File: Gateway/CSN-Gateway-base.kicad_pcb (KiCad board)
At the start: 2 copper layers, 32 x 85.5 mm, 0 parts

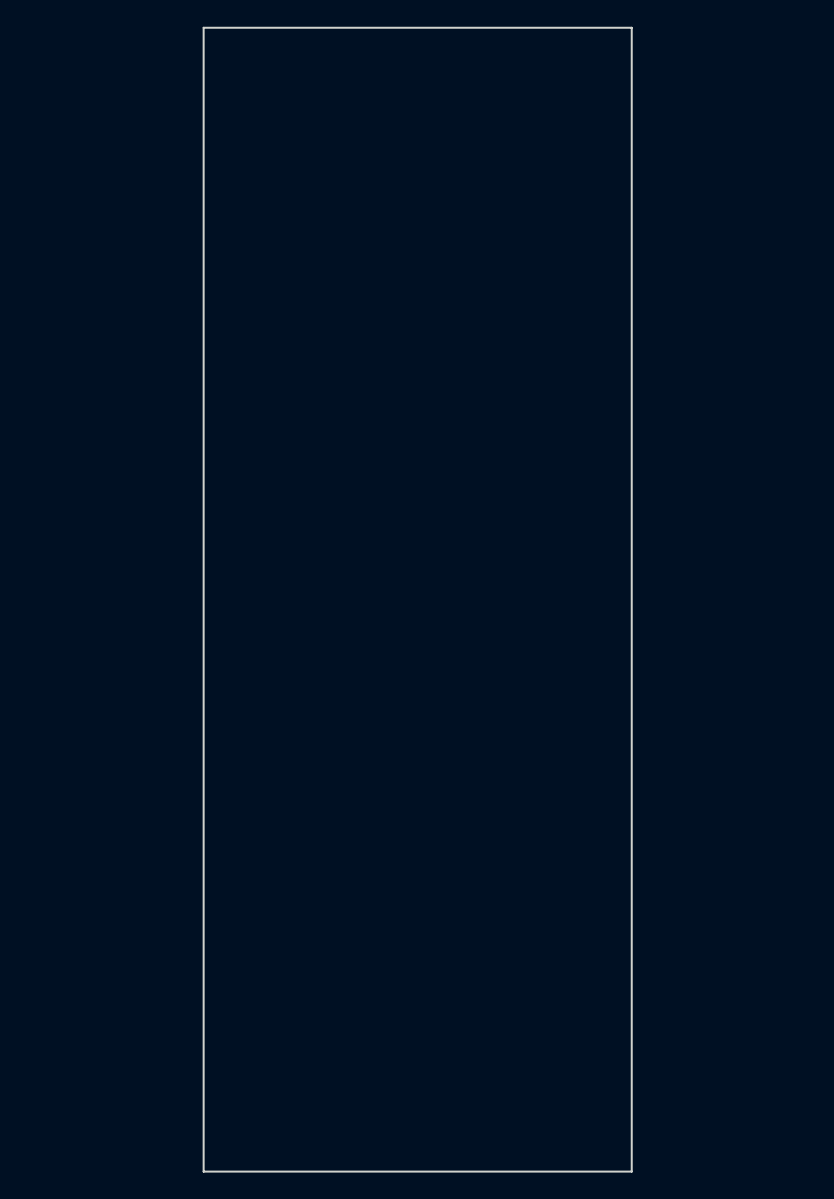
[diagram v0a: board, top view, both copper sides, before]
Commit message: add some pcb footprint
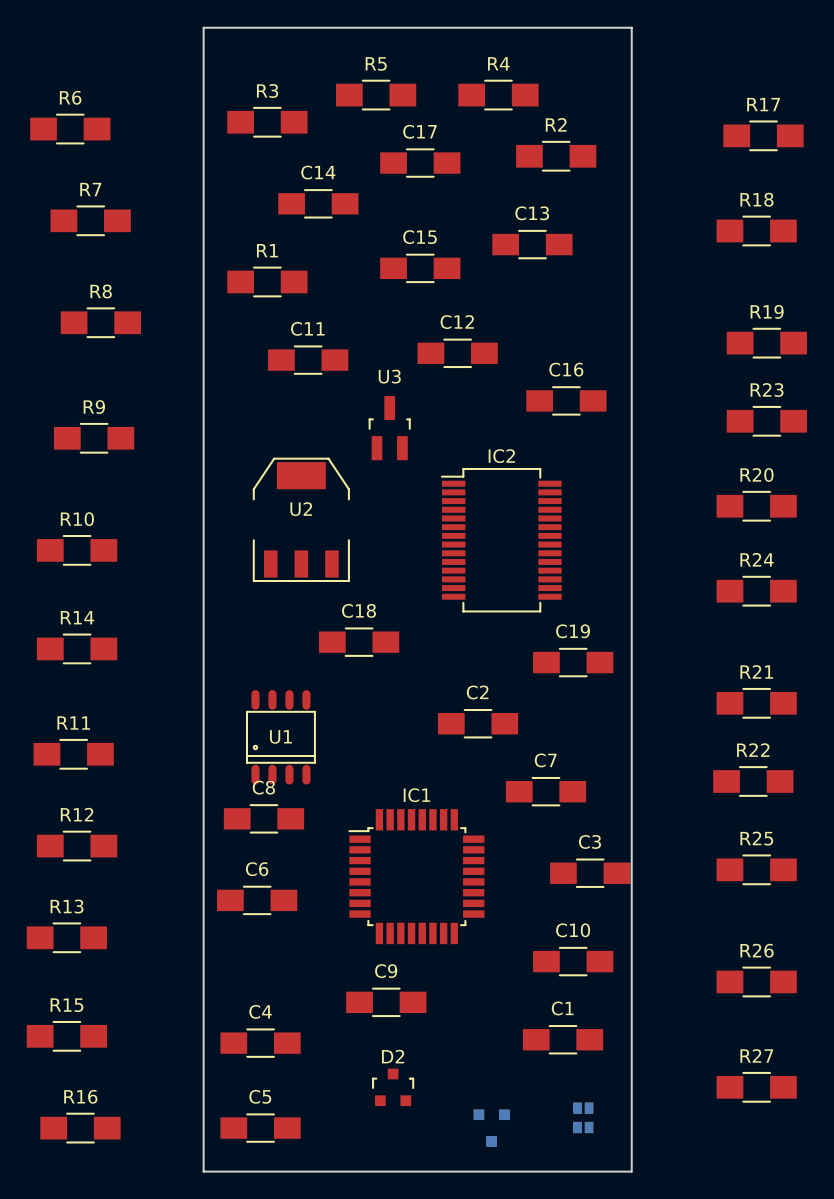
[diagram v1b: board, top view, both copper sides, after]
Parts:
- added C1: 0.1uF, Capacitors_SMD:C_1206_HandSoldering, F.Cu at (165.9, 136.1)
- added C10: 10uF, Capacitors_SMD:C_1206_HandSoldering, F.Cu at (166.6, 130.3)
- added C11: 0.1uF, Capacitors_SMD:C_1206_HandSoldering, F.Cu at (146.8, 85.3)
- added C12: 0.1uF, Capacitors_SMD:C_1206_HandSoldering, F.Cu at (158.0, 84.8)
- added C13: 10uF, Capacitors_SMD:C_1206_HandSoldering, F.Cu at (163.6, 76.7)
- added C14: 100nF, Capacitors_SMD:C_1206_HandSoldering, F.Cu at (147.6, 73.7)
- added C15: 100nF, Capacitors_SMD:C_1206_HandSoldering, F.Cu at (155.2, 78.5)
- added C16: 100nF, Capacitors_SMD:C_1206_HandSoldering, F.Cu at (166.1, 88.4)
- added C17: 10uF, Capacitors_SMD:C_1206_HandSoldering, F.Cu at (155.2, 70.6)
- added C18: 100nF, Capacitors_SMD:C_1206_HandSoldering, F.Cu at (150.6, 106.4)
- added C19: 100nF, Capacitors_SMD:C_1206_HandSoldering, F.Cu at (166.6, 108.0)
- added C2: 0.1uF, Capacitors_SMD:C_1206_HandSoldering, F.Cu at (159.5, 112.5)
- added C3: 22pF, Capacitors_SMD:C_1206_HandSoldering, F.Cu at (167.9, 123.7)
- added C4: 22pF, Capacitors_SMD:C_1206_HandSoldering, F.Cu at (143.3, 136.4)
- added C5: 10uF, Capacitors_SMD:C_1206_HandSoldering, F.Cu at (143.3, 142.7)
- added C6: 10uF, Capacitors_SMD:C_1206_HandSoldering, F.Cu at (143.0, 125.7)
- added C7: 10uF, Capacitors_SMD:C_1206_HandSoldering, F.Cu at (164.6, 117.6)
- added C8: 0.1uF, Capacitors_SMD:C_1206_HandSoldering, F.Cu at (143.5, 119.6)
- added C9: 10uF, Capacitors_SMD:C_1206_HandSoldering, F.Cu at (152.7, 133.3)
- added D1: LED_RABG, footprints:LED-0606, B.Cu at (167.4, 142.0)
- added D2: TL431, TO_SOT_Packages_SMD:SOT-23, F.Cu at (153.2, 139.7)
- added IC1: ATMEGA328-A, Housings_QFP:TQFP-32_7x7mm_Pitch0.8mm, F.Cu at (154.9, 124.0)
- added IC2: FT232RL, Housings_SSOP:SSOP-28_5.3x10.2mm_Pitch0.65mm, F.Cu at (161.3, 98.8)
- added Q1: 2N2222, TO_SOT_Packages_SMD:SOT-23, B.Cu at (160.5, 142.7)
- added R1: 10K, Resistors_SMD:R_1206_HandSoldering, F.Cu at (143.8, 79.5)
- added R10: 10K, Resistors_SMD:R_1206_HandSoldering, F.Cu at (129.5, 99.6)
- added R11: 10K, Resistors_SMD:R_1206_HandSoldering, F.Cu at (129.3, 114.8)
- added R12: 10K, Resistors_SMD:R_1206_HandSoldering, F.Cu at (129.5, 121.7)
- added R13: 10K, Resistors_SMD:R_1206_HandSoldering, F.Cu at (128.8, 128.5)
- added R14: 10KR, Resistors_SMD:R_1206_HandSoldering, F.Cu at (129.5, 106.9)
- added R15: 10K, Resistors_SMD:R_1206_HandSoldering, F.Cu at (128.8, 135.9)
- added R16: 100, Resistors_SMD:R_1206_HandSoldering, F.Cu at (129.8, 142.7)
- added R17: 20K, Resistors_SMD:R_1206_HandSoldering, F.Cu at (180.8, 68.6)
- added R18: 20K, Resistors_SMD:R_1206_HandSoldering, F.Cu at (180.3, 75.7)
- added R19: 120, Resistors_SMD:R_1206_HandSoldering, F.Cu at (181.1, 84.1)
- added R2: 33, Resistors_SMD:R_1206_HandSoldering, F.Cu at (165.4, 70.1)
- added R20: 4k7, Resistors_SMD:R_1206_HandSoldering, F.Cu at (180.3, 96.3)
- added R21: 10k, Resistors_SMD:R_1206_HandSoldering, F.Cu at (180.3, 111.0)
- added R22: 100, Resistors_SMD:R_1206_HandSoldering, F.Cu at (180.1, 116.8)
- added R23: 100, Resistors_SMD:R_1206_HandSoldering, F.Cu at (181.1, 89.9)
- added R24: 1.5K, Resistors_SMD:R_1206_HandSoldering, F.Cu at (180.3, 102.6)
- added R25: 27.4K, Resistors_SMD:R_1206_HandSoldering, F.Cu at (180.3, 123.4)
- added R26: 27.4K, Resistors_SMD:R_1206_HandSoldering, F.Cu at (180.3, 131.8)
- added R27: 10K, Resistors_SMD:R_1206_HandSoldering, F.Cu at (180.3, 139.7)
- added R3: 10K, Resistors_SMD:R_1206_HandSoldering, F.Cu at (143.8, 67.6)
- added R4: 10K, Resistors_SMD:R_1206_HandSoldering, F.Cu at (161.0, 65.5)
- added R5: 33, Resistors_SMD:R_1206_HandSoldering, F.Cu at (151.9, 65.5)
- added R6: 10K, Resistors_SMD:R_1206_HandSoldering, F.Cu at (129.0, 68.1)
- added R7: 10K, Resistors_SMD:R_1206_HandSoldering, F.Cu at (130.6, 74.9)
- added R8: 33, Resistors_SMD:R_1206_HandSoldering, F.Cu at (131.3, 82.5)
- added R9: 10K, Resistors_SMD:R_1206_HandSoldering, F.Cu at (130.8, 91.2)
- added U1: MAX485CSA, Power_Integrations:SO-8, F.Cu at (144.8, 113.5)
- added U2: AMS1117-3.3V, TO_SOT_Packages_SMD:SOT-223, F.Cu at (146.3, 97.3)
- added U3: ATSHA204A, TO_SOT_Packages_SMD:SOT-23_Handsoldering, F.Cu at (152.9, 90.4)

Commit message: change to 0806
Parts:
- C1, C10, C11, C12, C13, C14, C15, C16, C17, C18, C19, C2, C3, C4, C5, C6, C7, C8, C9: footprint Capacitors_SMD:C_1206_HandSoldering -> Capacitors_SMD:C_0805_HandSoldering
- R1, R10, R11, R12, R13, R14, R15, R16, R17, R18, R19, R2, R20, R21, R22, R23, R24, R25, R26, R27, R3, R4, R5, R6, R7, R8, R9: footprint Resistors_SMD:R_1206_HandSoldering -> Resistors_SMD:R_0805_HandSoldering
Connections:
- IC1 pad 13: CE -> (no net)
- IC1 pad 14: CSN -> (no net)
- IC1 pad 15: MOSI -> (no net)
- IC1 pad 16: MISO -> (no net)
- IC1 pad 17: SCK -> (no net)
- IC1 pad 22: Net-(IC1-Pad22) -> (no net)
- IC1 pad 28: SCL -> (no net)
- IC1 pad 32: IRQ -> (no net)
- IC2 pad 10: Net-(IC2-Pad10) -> (no net)
- IC2 pad 11: Net-(IC2-Pad11) -> (no net)
- IC2 pad 12: Net-(IC2-Pad12) -> (no net)
- IC2 pad 13: Net-(IC2-Pad13) -> (no net)
- IC2 pad 14: Net-(IC2-Pad14) -> (no net)
- IC2 pad 15: Net-(IC2-Pad15) -> (no net)
- IC2 pad 16: Net-(IC2-Pad16) -> (no net)
- IC2 pad 17: Net-(IC2-Pad17) -> (no net)
- IC2 pad 22: Net-(IC2-Pad22) -> (no net)
- IC2 pad 23: Net-(IC2-Pad23) -> (no net)
- IC2 pad 27: Net-(IC2-Pad27) -> (no net)
- IC2 pad 28: Net-(IC2-Pad28) -> (no net)
- IC2 pad 3: Net-(IC2-Pad3) -> (no net)
- IC2 pad 6: Net-(IC2-Pad6) -> (no net)
- IC2 pad 9: Net-(IC2-Pad9) -> (no net)
- R20 pad 1: Net-(P1-Pad1) -> (no net)

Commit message: Split project into 2 sch + 2 pcb (screen + base)
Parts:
- removed C15, C19: 100nF, Capacitors_SMD:C_0805_HandSoldering
- removed C2: 0.1uF, Capacitors_SMD:C_0805_HandSoldering
- removed D1: LED_RABG, footprints:LED-0606
- removed IC2: FT232RL, Housings_SSOP:SSOP-28_5.3x10.2mm_Pitch0.65mm
- removed R15, R27: 10K, Resistors_SMD:R_0805_HandSoldering
- removed R16, R22, R23: 100, Resistors_SMD:R_0805_HandSoldering
- removed R20: 4k7, Resistors_SMD:R_0805_HandSoldering
- removed R21: 10k, Resistors_SMD:R_0805_HandSoldering
- added C20: 10uF, Capacitors_SMD:C_0805_HandSoldering, F.Cu at (169.4, 150.6)
- added P3: CONN_ICSP, Pin_Headers:Pin_Header_Straight_2x03, F.Cu at (179.3, 144.3)
- added P8: CONN_NRF24L01, mysensors_radios:NRF24L01, F.Cu at (128.5, 139.4)
- added R28: 33, Resistors_SMD:R_0805_HandSoldering, F.Cu at (142.2, 151.9)
- added R29: 10K, Resistors_SMD:R_0805_HandSoldering, F.Cu at (180.6, 109.2)
- added R30: 10K, Resistors_SMD:R_0805_HandSoldering, F.Cu at (179.6, 90.4)
- added Y1: Crystal, mysensors_obscurities:XTAL_3.2x1.5mm, F.Cu at (179.8, 96.0)
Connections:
- net Net-(P9-Pad1) renamed RS485-A
- net Net-(P9-Pad2) renamed RS485-B
- IC1 pad 10: Net-(IC1-Pad10) -> (no net)
- IC1 pad 11: Net-(IC1-Pad11) -> (no net)
- IC1 pad 12: BTN1 -> (no net)
- IC1 pad 13: (no net) -> CE
- IC1 pad 14: (no net) -> CSN
- IC1 pad 15: (no net) -> MOSI
- IC1 pad 16: (no net) -> MISO
- IC1 pad 17: (no net) -> SCK
- IC1 pad 22: (no net) -> A3
- IC1 pad 25: BTN2 -> (no net)
- IC1 pad 26: Net-(IC1-Pad26) -> (no net)
- IC1 pad 30: RXI -> (no net)
- IC1 pad 31: TXO -> (no net)
- IC1 pad 32: (no net) -> IRQ

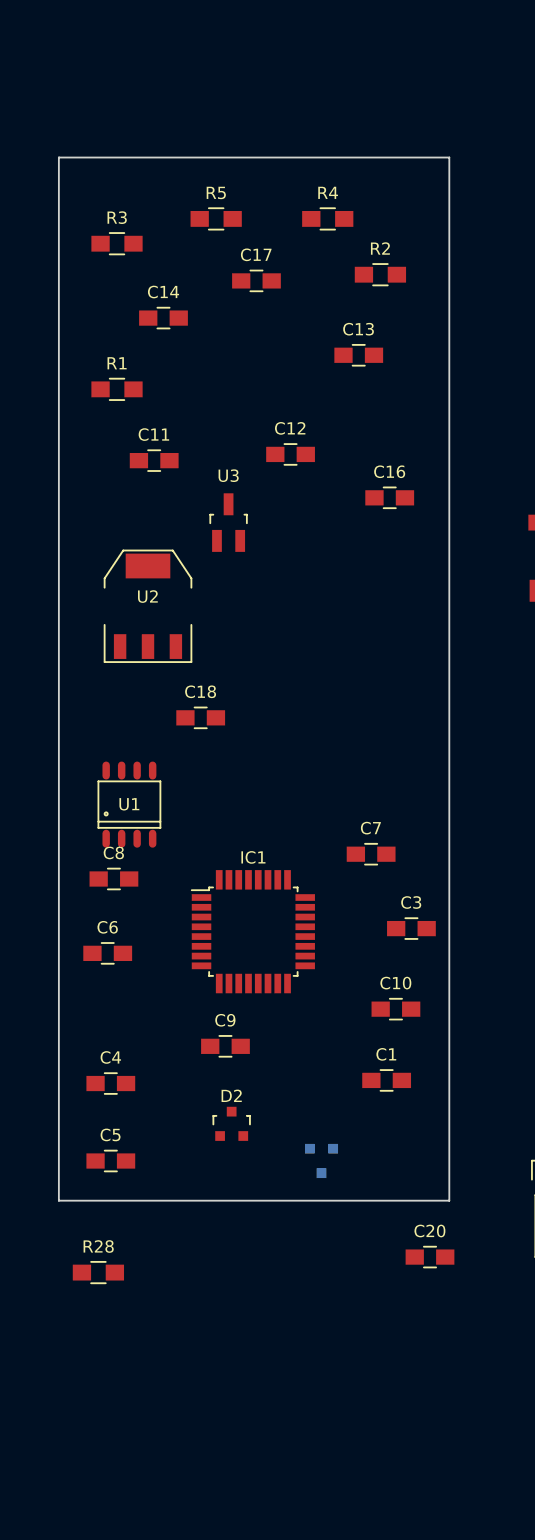
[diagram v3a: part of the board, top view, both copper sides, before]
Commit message: add multicomp footprint
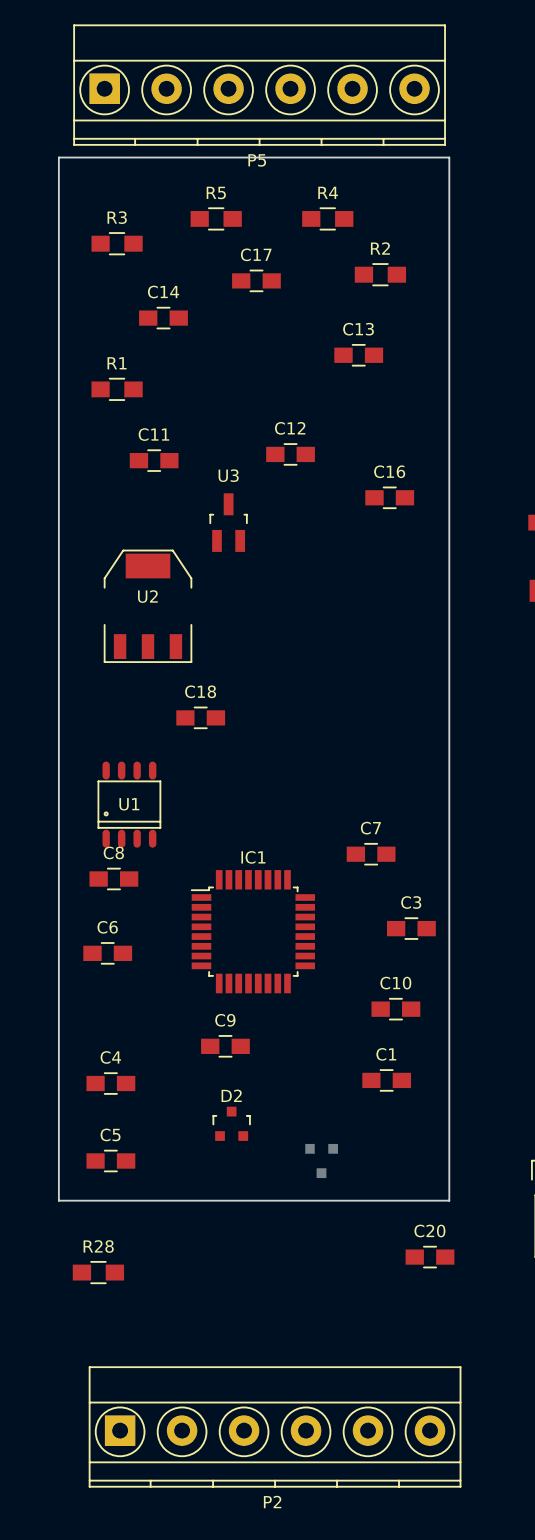
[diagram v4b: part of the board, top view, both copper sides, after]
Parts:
- added P2: CONN4, footprints:TerminalBlock_Multicomp-5-08-6pol, F.Cu at (144.0, 164.8)
- added P5: CONN6, footprints:TerminalBlock_Multicomp-5-08-6pol, F.Cu at (142.7, 54.9)
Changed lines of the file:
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@@
 (kicad_pcb (version 4) (host pcbnew 4.0.4-stable)
   (general
-    (links 110)
-    (no_connects 110)
+    (links 122)
+    (no_connects 122)
     (area 138.924999 60.424999 171.075001 146.075001)
     (thickness 1.6)
@@
     (tracks 0)
     (zones 0)
-    (modules 49)
+    (modules 51)
     (nets 31)
   )
@@
       (rotate (xyz 0 0 0))
     )
+  )
+  (module footprints:TerminalBlock_Multicomp-5-08-6pol (layer F.Cu)
+    (at 144.018 164.846)
+    (descr "6-way 5.08mm pitch terminal block, Multicomp MC000038")
+    (fp_text reference P2 (at 12.5 5.9) (layer F.SilkS)
+      (effects (font (size 1 1) (thickness 0.15)))
+    )
+    (fp_text value CONN4 (at 12.5 -6.6) (layer F.Fab)
+      (effects (font (size 1 1) (thickness 0.15)))
+    )
+    (fp_line (start -2.7 -5.4) (end 28.1 -5.4) (layer F.CrtYd) (width 0.05))
+    (fp_line (start -2.7 4.8) (end -2.7 -5.4) (layer F.CrtYd) (width 0.05))
+    (fp_line (start 28.1 4.8) (end -2.7 4.8) (layer F.CrtYd) (width 0.05))
+    (fp_line (start 28.1 -5.4) (end 28.1 4.8) (layer F.CrtYd) (width 0.05))
+    (fp_circle (center 25.4 0.1) (end 23.4 0.1) (layer F.SilkS) (width 0.15))
+    (fp_line (start 22.86 4.1) (end 22.86 4.6) (layer F.SilkS) (width 0.15))
+    (fp_line (start 17.78 4.1) (end 17.78 4.6) (layer F.SilkS) (width 0.15))
+    (fp_circle (center 20.32 0.1) (end 18.32 0.1) (layer F.SilkS) (width 0.15))
+    (fp_line (start 12.7 4.1) (end 12.7 4.6) (layer F.SilkS) (width 0.15))
+    (fp_circle (center 15.24 0.1) (end 13.24 0.1) (layer F.SilkS) (width 0.15))
+    (fp_circle (center 10.16 0.1) (end 8.16 0.1) (layer F.SilkS) (width 0.15))
+    (fp_line (start 7.62 4.1) (end 7.62 4.6) (layer F.SilkS) (width 0.15))
+    (fp_line (start 2.5 4.1) (end 2.5 4.6) (layer F.SilkS) (width 0.15))
+    (fp_circle (center 5.08 0.1) (end 3.08 0.1) (layer F.SilkS) (width 0.15))
+    (fp_circle (center 0 0.1) (end 2 0.1) (layer F.SilkS) (width 0.15))
+    (fp_line (start -2.5 2.6) (end 27.9 2.6) (layer F.SilkS) (width 0.15))
+    (fp_line (start -2.5 -2.3) (end 27.9 -2.3) (layer F.SilkS) (width 0.15))
+    (fp_line (start -2.5 4.1) (end 27.9 4.1) (layer F.SilkS) (width 0.15))
+    (fp_line (start -2.5 4.6) (end 27.9 4.6) (layer F.SilkS) (width 0.15))
+    (fp_line (start 27.9 4.6) (end 27.9 -5.2) (layer F.SilkS) (width 0.15))
+    (fp_line (start 27.9 -5.2) (end -2.5 -5.2) (layer F.SilkS) (width 0.15))
+    (fp_line (start -2.5 -5.2) (end -2.5 4.6) (layer F.SilkS) (width 0.15))
+    (pad 6 thru_hole circle (at 25.4 0) (size 2.5 2.5) (drill 1.3) (layers *.Cu *.Mask)
+      (net 21 CT1-A0))
+    (pad 5 thru_hole circle (at 20.32 0) (size 2.5 2.5) (drill 1.3) (layers *.Cu *.Mask)
+      (net 27 A3))
+    (pad 4 thru_hole circle (at 15.24 0) (size 2.5 2.5) (drill 1.3) (layers *.Cu *.Mask)
+      (net 29 RS485-A))
+    (pad 3 thru_hole circle (at 10.16 0) (size 2.5 2.5) (drill 1.3) (layers *.Cu *.Mask)
+      (net 30 RS485-B))
+    (pad 1 thru_hole rect (at 0 0) (size 2.5 2.5) (drill 1.3) (layers *.Cu *.Mask)
+      (net 2 GND))
+    (pad 2 thru_hole circle (at 5.08 0) (size 2.5 2.5) (drill 1.3) (layers *.Cu *.Mask)
+      (net 20 "Net-(P2-Pad2)"))
+    (model Terminal_Blocks.3dshapes/TerminalBlock_Pheonix_MKDS1.5-6pol.wrl
+      (at (xyz 0.4921 0 0))
+      (scale (xyz 1 1 1))
+      (rotate (xyz 0 0 0))
+    )
+  )
+  (module footprints:TerminalBlock_Multicomp-5-08-6pol (layer F.Cu)
+    (at 142.748 54.864)
+    (descr "6-way 5.08mm pitch terminal block, Multicomp MC000038")
+    (fp_text reference P5 (at 12.5 5.9) (layer F.SilkS)
+      (effects (font (size 1 1) (thickness 0.15)))
+    )
+    (fp_text value CONN6 (at 12.5 -6.6) (layer F.Fab)
+      (effects (font (size 1 1) (thickness 0.15)))
+    )
+    (fp_line (start -2.7 -5.4) (end 28.1 -5.4) (layer F.CrtYd) (width 0.05))
+    (fp_line (start -2.7 4.8) (end -2.7 -5.4) (layer F.CrtYd) (width 0.05))
+    (fp_line (start 28.1 4.8) (end -2.7 4.8) (layer F.CrtYd) (width 0.05))
+    (fp_line (start 28.1 -5.4) (end 28.1 4.8) (layer F.CrtYd) (width 0.05))
+    (fp_circle (center 25.4 0.1) (end 23.4 0.1) (layer F.SilkS) (width 0.15))
+    (fp_line (start 22.86 4.1) (end 22.86 4.6) (layer F.SilkS) (width 0.15))
+    (fp_line (start 17.78 4.1) (end 17.78 4.6) (layer F.SilkS) (width 0.15))
+    (fp_circle (center 20.32 0.1) (end 18.32 0.1) (layer F.SilkS) (width 0.15))
+    (fp_line (start 12.7 4.1) (end 12.7 4.6) (layer F.SilkS) (width 0.15))
+    (fp_circle (center 15.24 0.1) (end 13.24 0.1) (layer F.SilkS) (width 0.15))
+    (fp_circle (center 10.16 0.1) (end 8.16 0.1) (layer F.SilkS) (width 0.15))
+    (fp_line (start 7.62 4.1) (end 7.62 4.6) (layer F.SilkS) (width 0.15))
+    (fp_line (start 2.5 4.1) (end 2.5 4.6) (layer F.SilkS) (width 0.15))
+    (fp_circle (center 5.08 0.1) (end 3.08 0.1) (layer F.SilkS) (width 0.15))
+    (fp_circle (center 0 0.1) (end 2 0.1) (layer F.SilkS) (width 0.15))
+    (fp_line (start -2.5 2.6) (end 27.9 2.6) (layer F.SilkS) (width 0.15))
+    (fp_line (start -2.5 -2.3) (end 27.9 -2.3) (layer F.SilkS) (width 0.15))
+    (fp_line (start -2.5 4.1) (end 27.9 4.1) (layer F.SilkS) (width 0.15))
+    (fp_line (start -2.5 4.6) (end 27.9 4.6) (layer F.SilkS) (width 0.15))
+    (fp_line (start 27.9 4.6) (end 27.9 -5.2) (layer F.SilkS) (width 0.15))
+    (fp_line (start 27.9 -5.2) (end -2.5 -5.2) (layer F.SilkS) (width 0.15))
+    (fp_line (start -2.5 -5.2) (end -2.5 4.6) (layer F.SilkS) (width 0.15))
+    (pad 6 thru_hole circle (at 25.4 0) (size 2.5 2.5) (drill 1.3) (layers *.Cu *.Mask)
+      (net 16 A2))
+    (pad 5 thru_hole circle (at 20.32 0) (size 2.5 2.5) (drill 1.3) (layers *.Cu *.Mask)
+      (net 7 "Net-(C6-Pad1)"))
+    (pad 4 thru_hole circle (at 15.24 0) (size 2.5 2.5) (drill 1.3) (layers *.Cu *.Mask)
+      (net 18 A1))
+    (pad 3 thru_hole circle (at 10.16 0) (size 2.5 2.5) (drill 1.3) (layers *.Cu *.Mask)
+      (net 8 "Net-(C7-Pad1)"))
+    (pad 1 thru_hole rect (at 0 0) (size 2.5 2.5) (drill 1.3) (layers *.Cu *.Mask)
+      (net 6 "Net-(C5-Pad1)"))
+    (pad 2 thru_hole circle (at 5.08 0) (size 2.5 2.5) (drill 1.3) (layers *.Cu *.Mask)
+      (net 17 A0))
+    (model Terminal_Blocks.3dshapes/TerminalBlock_Pheonix_MKDS1.5-6pol.wrl
+      (at (xyz 0.4921 0 0))
+      (scale (xyz 1 1 1))
+      (rotate (xyz 0 0 0))
+    )
